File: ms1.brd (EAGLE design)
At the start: 100 x 100 mm, 125 parts, among them IC1 MAX3232EUE, J1 POWERPOLE_POWER25A, J10 RS485, J11 I2C, J12 TTL_SERIAL, J13 Radio, J14 RS232, J2 RAIN, J3 ADC1, J4 ON, J5 D1, J6 D2, J7 ADC2, J8 LED-EN, Q1 DMG6602SVT, Q2 DMG6602SVT, Q3 DMG6602SVT, Q4 DMG6602SVT, U1 LT1934ES6TRMPBF, U2 LT1934ES6TRMPBF, U3 DS3231SN, U4 ISL3179EIBZ, X1 KUSBVX-BS1N

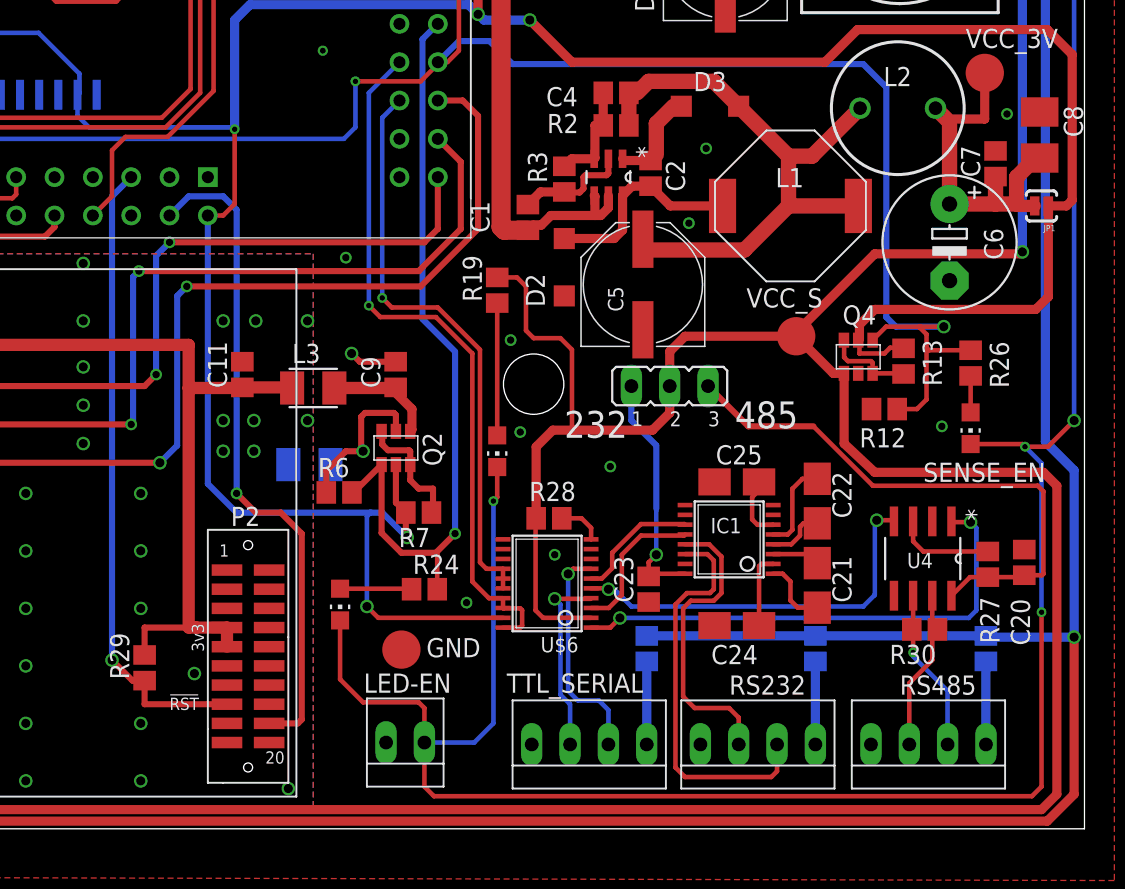
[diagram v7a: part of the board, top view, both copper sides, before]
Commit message: DIO remapped to be TXEN for rs485, new DIO pin not yet selected
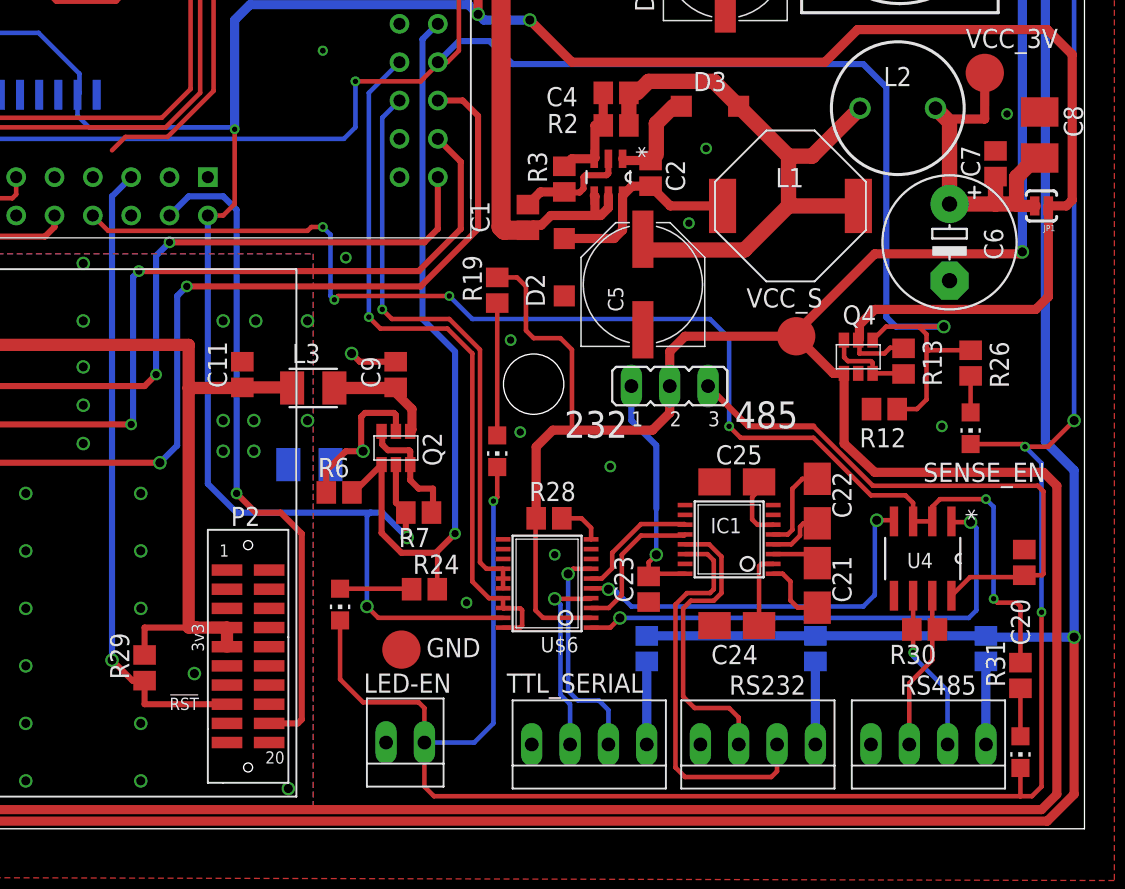
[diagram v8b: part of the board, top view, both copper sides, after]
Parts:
- removed R27: 1K, resistor:R0805
- added LED12: TXEN, led:CHIP-LED0805
- added R31: 56, resistor:R0805
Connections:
- removed net N$10: R27.1, U4.3
- new net N$27: LED12.A, R31.1
- new net TXEN: R31.2, U$5.C46, U4.2, U4.3
- net 485_3V3: no longer R27.2
- net DIO_2: no longer U$5.C46
- net GND: no longer U4.2
- net LGND: now also LED12.C
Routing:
- net TXEN: track 0.00 -> 88.2 mm, vias 0 -> 6
- net N$10: track 6.55 -> 0.00 mm
- net DIO_2: track 106.0 -> 101.1 mm
- net N$27: track 0.00 -> 3.18 mm
- net LGND: track 378.6 -> 380.5 mm
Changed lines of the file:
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@@
 <attribute name="NAME" x="95.123" y="15.24" size="1.27" layer="25" rot="R270"/>
-</element>
-<element name="R27" library="resistor" package="R0805" value="1K" x="93.599" y="17.526" smashed="yes" rot="R270">
-<attribute name="NAME" x="93.091" y="15.367" size="1.27" layer="25" rot="R270"/>
 </element>
 <element name="JP3" library="SparkFun-Passives" package="SJ_2S" value="" x="15.3035" y="67.5005" rot="R180"/>
@@
 <element name="JP5" library="jumper" package="JP1" value="GND-LINK" x="30.988" y="88.9" smashed="yes" rot="R90">
 <attribute name="VALUE" x="38.1" y="85.725" size="1.27" layer="27" ratio="10" rot="R180"/>
+</element>
+<element name="LED12" library="led" package="CHIP-LED0805" value="TXEN" x="95.758" y="5.08" smashed="yes" rot="R180">
+<attribute name="VALUE" x="97.028" y="6.858" size="1.27" layer="27" rot="R270"/>
+</element>
+<element name="R31" library="resistor" package="R0805" value="56" x="95.758" y="10.16" smashed="yes" rot="R90">
+<attribute name="NAME" x="94.742" y="9.398" size="1.27" layer="25" rot="R90"/>
 </element>
 </elements>
@@
 <contactref element="C19" pad="1"/>
 <contactref element="U4" pad="5"/>
-<contactref element="U4" pad="2"/>
 <contactref element="C20" pad="2"/>
 <contactref element="IC1" pad="15"/>
@@
 <wire x1="56.261" y1="5.715" x2="56.261" y2="2.794" width="0.3048" layer="1"/>
 <wire x1="56.261" y1="2.794" x2="56.896" y2="2.159" width="0.3048" layer="1"/>
-<wire x1="56.896" y1="2.159" x2="96.52" y2="2.159" width="0.3048" layer="1"/>
+<wire x1="56.896" y1="2.159" x2="95.758" y2="2.159" width="0.3048" layer="1"/>
+<wire x1="95.758" y1="2.159" x2="96.52" y2="2.159" width="0.3048" layer="1"/>
 <wire x1="96.52" y1="2.159" x2="97.155" y2="2.794" width="0.3048" layer="1"/>
 <wire x1="97.155" y1="2.794" x2="97.155" y2="14.351" width="0.3048" layer="1"/>
@@
 <wire x1="60.833" y1="6.985" x2="59.563" y2="5.715" width="0.3048" layer="16"/>
 <wire x1="59.563" y1="5.715" x2="56.261" y2="5.715" width="0.3048" layer="16"/>
+<contactref element="LED12" pad="C"/>
+<wire x1="95.758" y1="4.03" x2="95.758" y2="2.159" width="0.3048" layer="1"/>
 </signal>
 <signal name="N$16">
@@
 <wire x1="90.678" y1="90.932" x2="90.043" y2="90.297" width="0.6096" layer="1"/>
 <wire x1="90.043" y1="90.297" x2="90.043" y2="89.027" width="0.6096" layer="1"/>
-<contactref element="U$5" pad="C46"/>
 <wire x1="90.043" y1="89.027" x2="90.043" y2="81.28" width="0.3048" layer="16"/>
 <wire x1="90.043" y1="81.28" x2="89.027" y2="80.264" width="0.3048" layer="16"/>
@@
 <wire x1="39.243" y1="45.847" x2="36.449" y2="45.847" width="0.3048" layer="1"/>
 <wire x1="36.449" y1="45.847" x2="35.56" y2="44.958" width="0.3048" layer="1"/>
-<wire x1="35.56" y1="44.958" x2="35.56" y2="41.91" width="0.3048" layer="1"/>
-<wire x1="35.56" y1="41.91" x2="34.29" y2="40.64" width="0.3048" layer="1"/>
+<wire x1="35.56" y1="44.958" x2="35.56" y2="41.91" width="0" layer="19" extent="1-16"/>
 </signal>
 <signal name="N$23">
@@
 <wire x1="60.366" y1="17.231" x2="59.944" y2="17.653" width="0.3048" layer="1"/>
 <wire x1="59.944" y1="17.653" x2="59.944" y2="31.75" width="0.3048" layer="1"/>
-<wire x1="59.944" y1="31.75" x2="57.15" y2="34.544" width="0.3048" layer="1"/>
-<wire x1="57.15" y1="34.544" x2="54.102" y2="34.544" width="0.3048" layer="1"/>
-<wire x1="54.102" y1="34.544" x2="53.467" y2="35.179" width="0.3048" layer="1"/>
-<via x="53.467" y="35.179" extent="1-16" drill="0.3556"/>
-<wire x1="53.467" y1="35.179" x2="53.467" y2="47.117" width="0.3048" layer="16"/>
+<wire x1="59.944" y1="31.75" x2="57.912" y2="33.782" width="0.3048" layer="1"/>
+<wire x1="57.912" y1="33.782" x2="54.102" y2="33.782" width="0.3048" layer="1"/>
+<wire x1="54.102" y1="33.782" x2="53.467" y2="34.417" width="0.3048" layer="1"/>
+<via x="53.467" y="34.417" extent="1-16" drill="0.3556"/>
+<wire x1="53.467" y1="34.417" x2="53.467" y2="47.117" width="0.3048" layer="16"/>
 <wire x1="53.467" y1="47.117" x2="54.61" y2="48.26" width="0.3048" layer="16"/>
 </signal>
@@
 <wire x1="60.538" y1="15.281" x2="59.436" y2="16.383" width="0.3048" layer="1"/>
 <wire x1="59.436" y1="16.383" x2="59.436" y2="31.496" width="0.3048" layer="1"/>
-<wire x1="59.436" y1="31.496" x2="57.023" y2="33.909" width="0.3048" layer="1"/>
-<wire x1="57.023" y1="33.909" x2="53.34" y2="33.909" width="0.3048" layer="1"/>
-<wire x1="53.34" y1="33.909" x2="52.578" y2="34.671" width="0.3048" layer="1"/>
-<via x="52.578" y="34.671" extent="1-16" drill="0.3556"/>
-<wire x1="52.578" y1="34.671" x2="52.578" y2="48.768" width="0.3048" layer="16"/>
+<wire x1="59.436" y1="31.496" x2="57.785" y2="33.147" width="0.3048" layer="1"/>
+<wire x1="57.785" y1="33.147" x2="53.34" y2="33.147" width="0.3048" layer="1"/>
+<wire x1="53.34" y1="33.147" x2="52.578" y2="33.909" width="0.3048" layer="1"/>
+<via x="52.578" y="33.909" extent="1-16" drill="0.3556"/>
+<wire x1="52.578" y1="33.909" x2="52.578" y2="48.768" width="0.3048" layer="16"/>
 <wire x1="52.578" y1="48.768" x2="54.61" y2="50.8" width="0.3048" layer="16"/>
 </signal>
@@
 <wire x1="68.453" y1="7.874" x2="68.453" y2="5.588" width="0.3048" layer="16"/>
 </signal>
-<signal name="N$10">
-<contactref element="U4" pad="3"/>
-<contactref element="R27" pad="1"/>
-<wire x1="93.599" y1="18.376" x2="89.32" y2="18.376" width="0.3048" layer="1"/>
-<wire x1="89.32" y1="18.376" x2="88.646" y2="19.05" width="0.3048" layer="1"/>
-<wire x1="88.646" y1="19.05" x2="88.646" y2="20.3708" width="0.3048" layer="1"/>
-</signal>
 <signal name="N$59">
 <contactref element="C22" pad="-"/>
@@
 <contactref element="U4" pad="8"/>
 <contactref element="C20" pad="1"/>
-<contactref element="R27" pad="2"/>
-<wire x1="93.599" y1="16.676" x2="92.4188" y2="16.676" width="0.3048" layer="1"/>
 <wire x1="92.4188" y1="16.676" x2="91.186" y2="15.4432" width="0.3048" layer="1"/>
-<wire x1="93.599" y1="16.676" x2="95.885" y2="16.676" width="0.3048" layer="1"/>
-<wire x1="95.885" y1="16.676" x2="96.012" y2="16.803" width="0.3048" layer="1"/>
 <wire x1="96.012" y1="16.803" x2="97.194" y2="16.803" width="0.3048" layer="1"/>
 <wire x1="97.194" y1="16.803" x2="97.282" y2="16.891" width="0.3048" layer="1"/>
@@
 <wire x1="82.042" y1="26.67" x2="77.724" y2="26.67" width="0.4064" layer="1"/>
 <wire x1="77.724" y1="26.67" x2="75.057" y2="29.337" width="0.4064" layer="1"/>
+<wire x1="92.4188" y1="16.676" x2="95.885" y2="16.676" width="0.3048" layer="1"/>
+<wire x1="95.885" y1="16.676" x2="96.012" y2="16.803" width="0.3048" layer="1"/>
 </signal>
 <signal name="N$8">
@@
 <wire x1="69.977" y1="27.051" x2="69.977" y2="29.337" width="0.4064" layer="16"/>
 </signal>
+<signal name="N$27">
+<contactref element="LED12" pad="A"/>
+<contactref element="R31" pad="1"/>
+<wire x1="95.758" y1="6.13" x2="95.758" y2="9.31" width="0.3048" layer="1"/>
+</signal>
+<signal name="TXEN">
+<contactref element="R31" pad="2"/>
+<contactref element="U4" pad="2"/>
+<contactref element="U4" pad="3"/>
+<contactref element="U$5" pad="C46"/>
+<wire x1="95.758" y1="11.01" x2="95.758" y2="14.732" width="0.3048" layer="1"/>
+<wire x1="95.758" y1="14.732" x2="95.504" y2="14.986" width="0.3048" layer="1"/>
+<wire x1="95.504" y1="14.986" x2="94.234" y2="14.986" width="0.3048" layer="1"/>
+<wire x1="94.234" y1="14.986" x2="93.98" y2="15.24" width="0.3048" layer="1"/>
+<via x="93.98" y="15.24" extent="1-16" drill="0.3556"/>
+<wire x1="93.98" y1="15.24" x2="93.98" y2="21.336" width="0.3048" layer="16"/>
+<wire x1="93.98" y1="21.336" x2="93.472" y2="21.844" width="0.3048" layer="16"/>
+<via x="93.472" y="21.844" extent="1-16" drill="0.3556"/>
+<wire x1="93.472" y1="21.844" x2="90.424" y2="21.844" width="0.3048" layer="1"/>
+<wire x1="90.424" y1="21.844" x2="89.916" y2="21.336" width="0.3048" layer="1"/>
+<wire x1="89.916" y1="21.336" x2="89.916" y2="20.3708" width="0.3048" layer="1"/>
+<wire x1="89.916" y1="20.3708" x2="88.646" y2="20.3708" width="0.3048" layer="1"/>
+<wire x1="88.646" y1="20.3708" x2="88.646" y2="21.59" width="0.3048" layer="1"/>
+<wire x1="88.646" y1="21.59" x2="88.138" y2="22.098" width="0.3048" layer="1"/>
+<wire x1="88.138" y1="22.098" x2="85.852" y2="22.098" width="0.3048" layer="1"/>
+<wire x1="85.852" y1="22.098" x2="82.042" y2="25.908" width="0.3048" layer="1"/>
+<wire x1="82.042" y1="25.908" x2="77.216" y2="25.908" width="0.3048" layer="1"/>
+<wire x1="77.216" y1="25.908" x2="76.454" y2="26.67" width="0.3048" layer="1"/>
+<via x="76.454" y="26.67" extent="1-16" drill="0.3556"/>
+<wire x1="76.454" y1="26.67" x2="76.454" y2="32.512" width="0.3048" layer="16"/>
+<wire x1="76.454" y1="32.512" x2="75.184" y2="33.782" width="0.3048" layer="16"/>
+<wire x1="75.184" y1="33.782" x2="59.436" y2="33.782" width="0.3048" layer="16"/>
+<wire x1="59.436" y1="33.782" x2="57.912" y2="35.306" width="0.3048" layer="16"/>
+<via x="57.912" y="35.306" extent="1-16" drill="0.3556"/>
+<wire x1="57.912" y1="35.306" x2="50.546" y2="35.306" width="0.3048" layer="1"/>
+<wire x1="50.546" y1="35.306" x2="50.292" y2="35.052" width="0.3048" layer="1"/>
+<via x="50.292" y="35.052" extent="1-16" drill="0.3556"/>
+<wire x1="50.292" y1="35.052" x2="50.038" y2="35.306" width="0.3048" layer="16"/>
+<wire x1="50.038" y1="35.306" x2="50.038" y2="39.37" width="0.3048" layer="16"/>
+<wire x1="50.038" y1="39.37" x2="49.53" y2="39.878" width="0.3048" layer="16"/>
+<via x="49.53" y="39.878" extent="1-16" drill="0.3556"/>
+<wire x1="49.53" y1="39.878" x2="48.768" y2="39.878" width="0.3048" layer="1"/>
+<wire x1="48.768" y1="39.878" x2="48.514" y2="39.624" width="0.3048" layer="1"/>
+<wire x1="48.514" y1="39.624" x2="35.306" y2="39.624" width="0.3048" layer="1"/>
+<wire x1="35.306" y1="39.624" x2="34.29" y2="40.64" width="0.3048" layer="1"/>
+</signal>
 </signals>
